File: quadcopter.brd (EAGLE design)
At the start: 140 x 140 mm, 65 parts, among them J1 AVR_SPI_PRG_6NS, Q1 N-CHANNEL_MOSFET, Q2 N-CHANNEL_MOSFET, Q3 N-CHANNEL_MOSFET, Q4 N-CHANNEL_MOSFET, U1 ATMEGA128RFA1

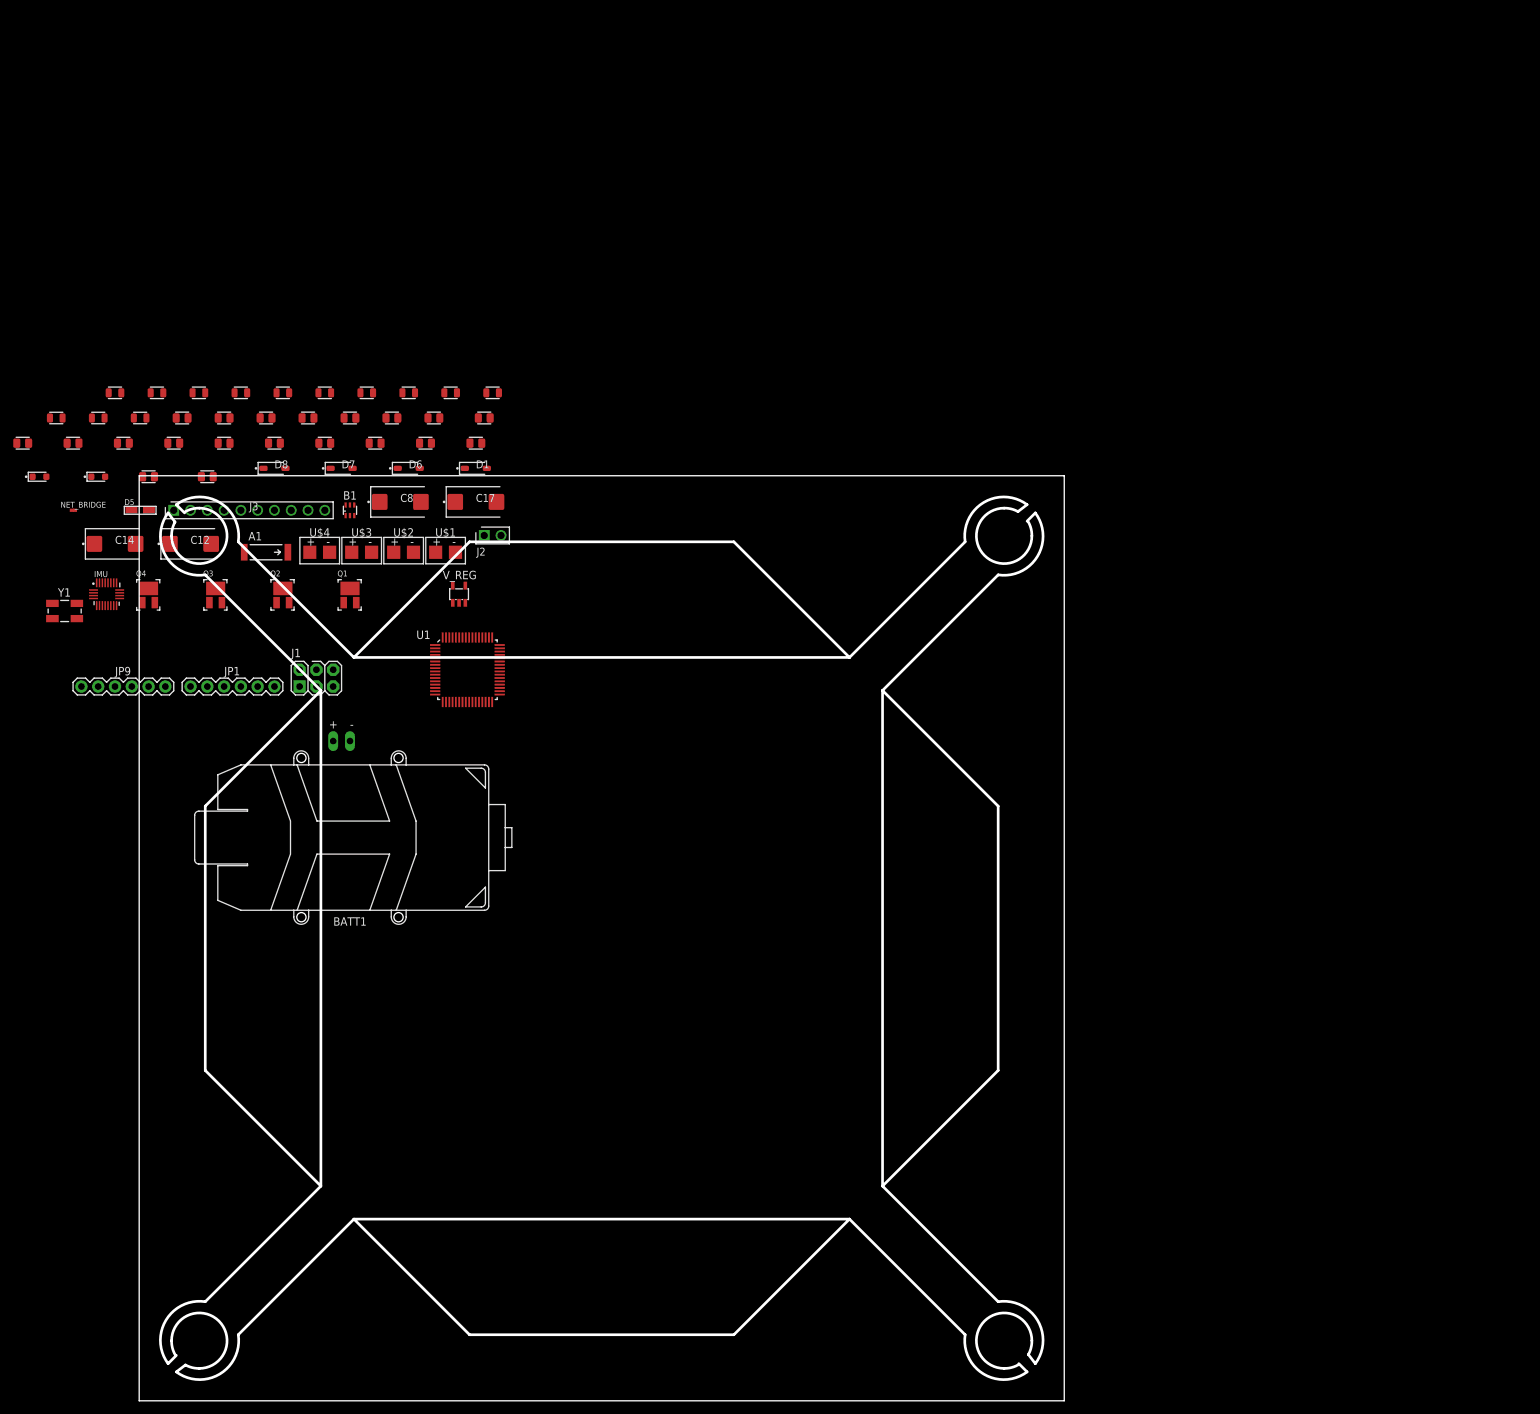
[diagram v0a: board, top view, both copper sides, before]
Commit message: Did board work, renamed flyback and filtered in schematic
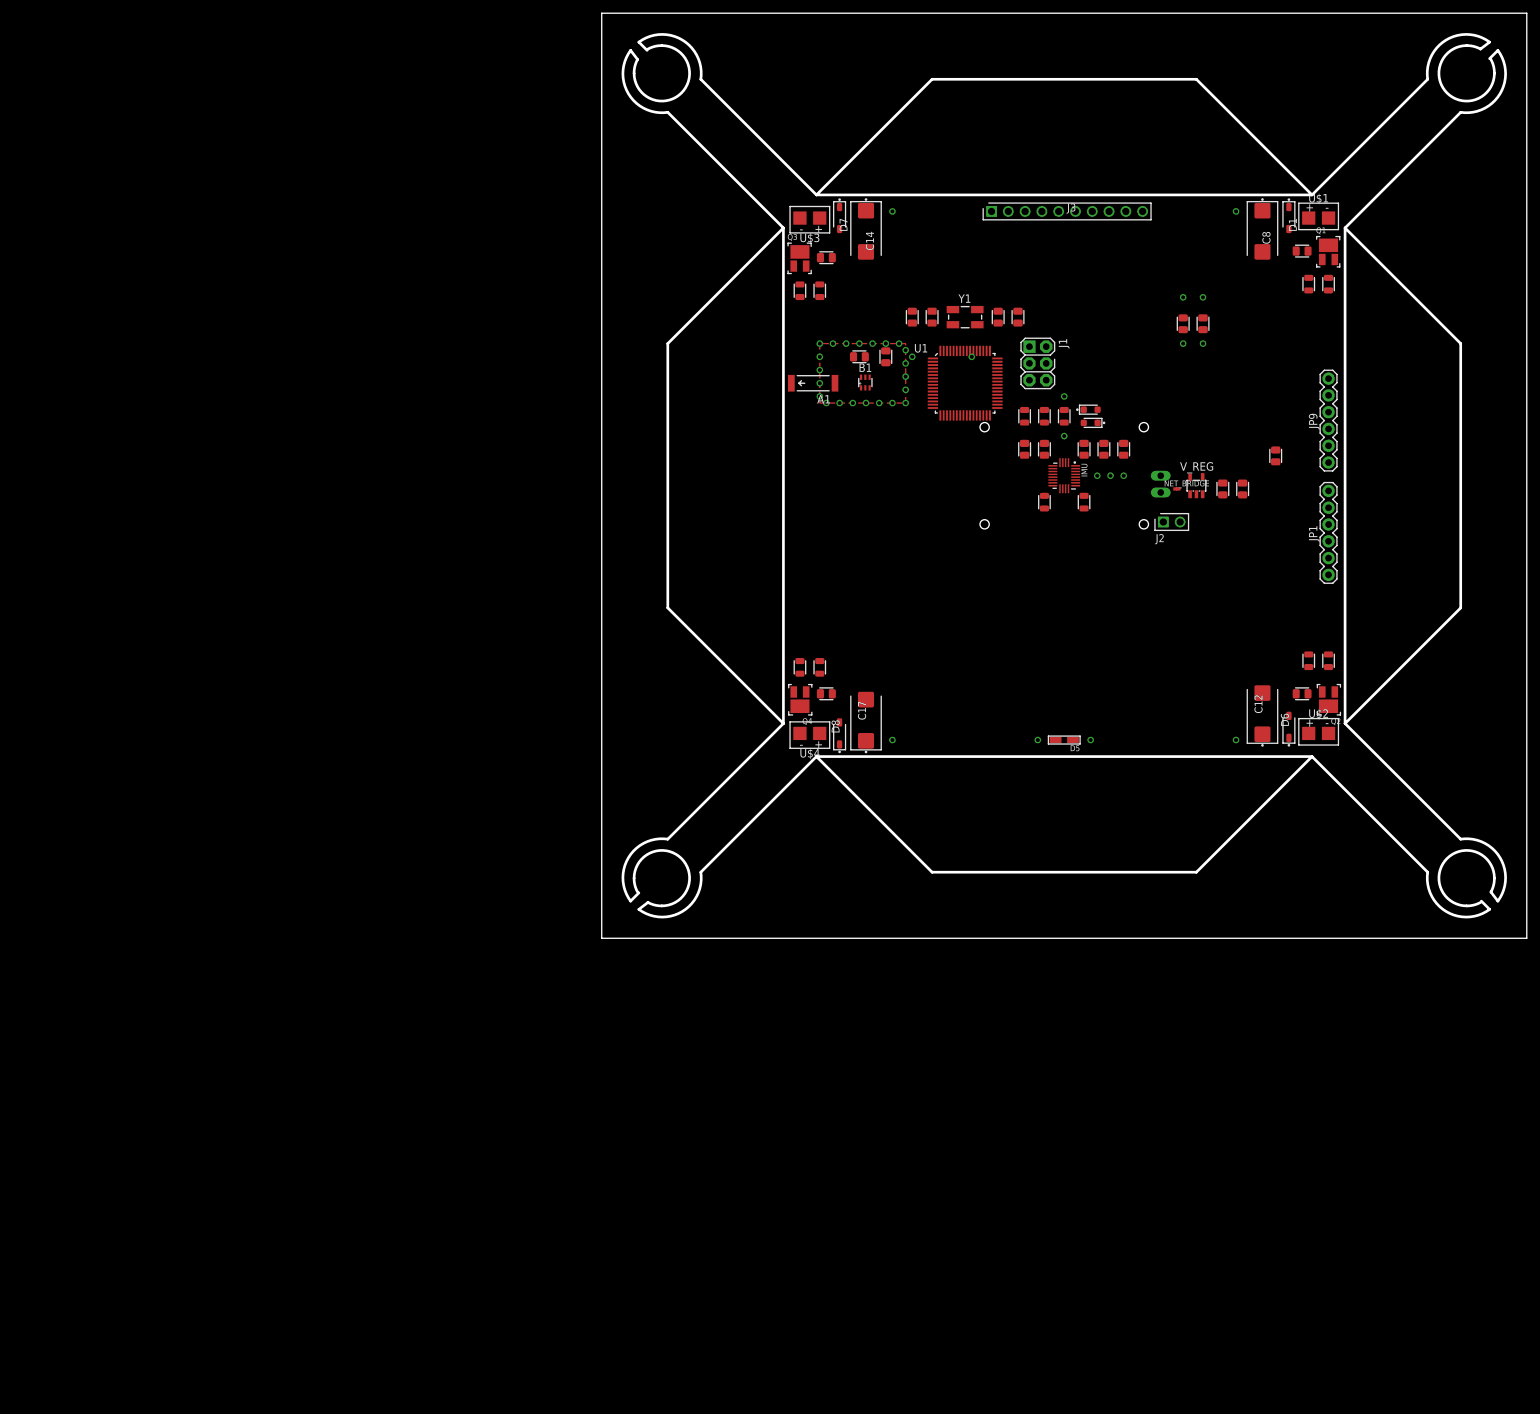
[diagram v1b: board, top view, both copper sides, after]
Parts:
- moved JP9 191.8 mm to (110.0, 72.0), turned to 90 degrees
- moved R3 190.6 mm to (107.0, 99.0), turned to 90 degrees
- moved R2 187.3 mm to (110.0, 99.0), turned to 90 degrees
- moved JP1 173.1 mm to (110.0, 55.0), turned to 90 degrees
- moved NET_BRIDGE 167.0 mm to (87.0, 68.0)
- moved C12 164.3 mm to (100.0, 34.0), turned to 90 degrees
- moved C24 160.9 mm to (97.0, 68.0), turned to 90 degrees
- moved LED3 159.4 mm to (74.0, 80.0)
- moved Q2 159.1 mm to (110.0, 36.0), turned to 180 degrees
- moved Q1 156.9 mm to (110.0, 104.0)
- moved C23 151.5 mm to (94.0, 68.0), turned to 90 degrees
- moved C22 151.4 mm to (79.0, 74.0), turned to 90 degrees
- moved LED2 150.4 mm to (74.0, 78.0), turned to 180 degrees
- moved C6 148.9 mm to (60.0, 94.0), turned to 90 degrees
- moved R7 148.2 mm to (107.0, 42.0), turned to 270 degrees
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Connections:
- removed net FILTERED: Q1.1, Q2.1, Q3.1, Q4.1, R10.2, R11.2, R2.2, R3.2, R4.2, R7.2, R8.2, R9.2
- removed net FLYBACK: D1.A, D6.A, D7.A, D8.A, Q1.3, Q2.3, Q3.3, Q4.3, U$1.V-, U$2.V-, U$3.V-, U$4.V-
- new net FILTERED1: Q1.1, R2.2, R3.2
- new net FILTERED2: Q2.1, R4.2, R7.2
- new net FILTERED3: Q3.1, R8.2, R9.2
- new net FILTERED4: Q4.1, R10.2, R11.2
- new net FLYBACK1: D1.A, Q1.3, U$1.V-
- new net FLYBACK2: D6.A, Q2.3, U$2.V-
- new net FLYBACK3: D7.A, Q3.3, U$3.V-
- new net FLYBACK4: D8.A, Q4.3, U$4.V-
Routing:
- added copper zone on layer 1, net GND
- added copper zone on layer 15, net GND
- added copper zone on layer 2, net GND
- added copper zone on layer 2, net VBAT
- added copper zone on layer 2, net VCC

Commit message: board before auto-routing
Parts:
- moved C24 6.37 mm to (92.8, 72.8), turned to 0 degrees
- moved C23 4.04 mm to (92.5, 64.2), turned to 0 degrees
- moved C21 3.82 mm to (76.8, 70.2)
- moved C18 3.51 mm to (63.8, 70.5)
- moved C20 2.85 mm to (75.8, 74.8)
- moved NET_BRIDGE 2.80 mm to (89.5, 69.2), turned to 270 degrees
- moved V_REG 2.75 mm to (92.8, 68.5)
- moved C19 2.61 mm to (64.5, 74.8)
- moved R13 2.57 mm to (75.2, 64.8)
- moved R12 2.36 mm to (65.0, 64.8)
- moved C9 1.82 mm to (37.2, 87.5), turned to 90 degrees
- moved Y1 1.25 mm to (55.0, 95.2)
- moved A1 0.75 mm to (32.0, 83.2)
- moved C11 0.71 mm to (42.5, 87.5)
- moved C22 0.25 mm to (79.0, 74.2)
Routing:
- added copper zone on layer 2, net N$20
- added copper zone on layer 15, net N$21
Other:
- board size 140 x 140 mm -> 133.6 x 133.6 mm
- board text added: "(res)"
- board text added: "BAT_GND"
- board text added: "DTR"
- board text added: "GND"
- board text added: "PWM1"
- board text added: "PWM2"
- board text added: "PWM3"
- board text added: "PWM4"
- board text added: "RXI"
- board text added: "SCL"
- board text added: "SDA"
- board text added: "TX0"
- board text added: "VBAT"
- board text added: "VCC"

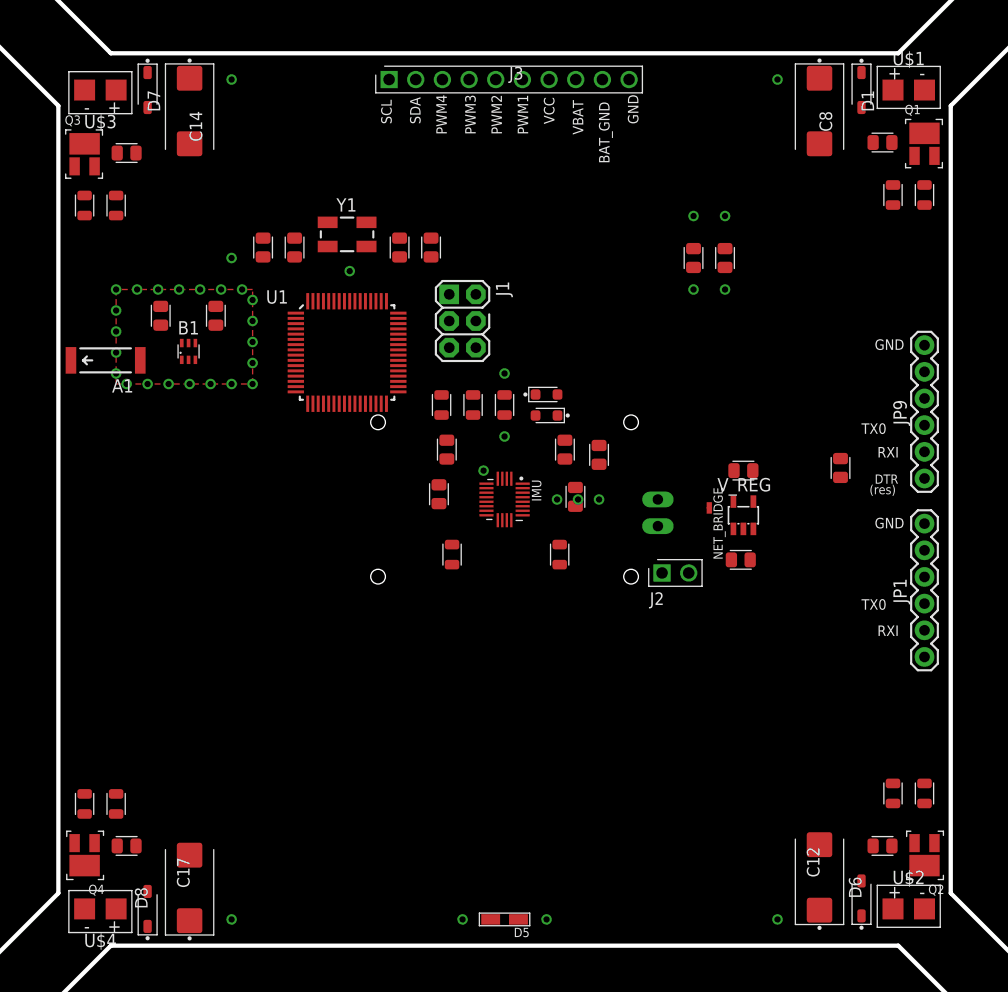
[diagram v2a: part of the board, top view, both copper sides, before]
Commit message: Routed and manually connected most wires. Waiting on piazza question before connecting the last few
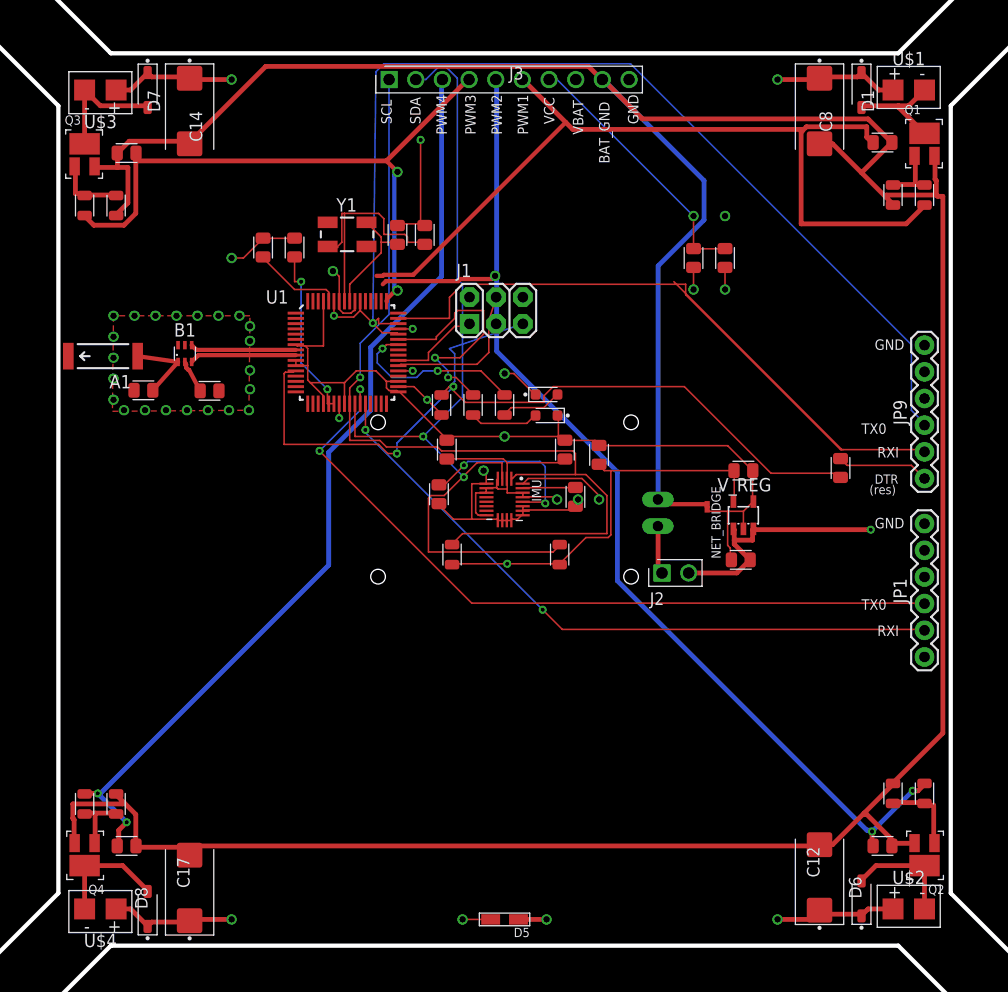
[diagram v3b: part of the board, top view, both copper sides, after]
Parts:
- moved C9 7.29 mm to (35.6, 80.4), turned to 180 degrees
- moved C11 7.18 mm to (41.9, 80.3), turned to 180 degrees
- moved J1 3.35 mm to (69.2, 88.0), turned to 0 degrees
- moved C5 1.34 mm to (62.4, 95.2)
- moved C6 1.22 mm to (59.8, 95.2)
- moved A1 0.47 mm to (31.8, 83.7)
- moved B1 0.40 mm to (39.5, 83.9)
- moved NET_BRIDGE 0.22 mm to (89.3, 69.3)
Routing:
- net BAT_GND: track 0.00 -> 318.6 mm
- net GND: track 0.00 -> 143.4 mm, vias 30 -> 32
- net VCC: track 0.00 -> 116.1 mm, vias 5 -> 9
- net PWM2: track 0.00 -> 106.3 mm, vias 0 -> 3
- net RX0: track 0.00 -> 97.6 mm, vias 0 -> 1
- net PWM4: track 0.00 -> 89.7 mm, vias 0 -> 2
- net SCL: track 0.00 -> 88.9 mm, vias 0 -> 1
- net SDA: track 0.00 -> 83.9 mm, vias 0 -> 2
- net RESET: track 0.00 -> 82.9 mm, vias 0 -> 2
- net TX0: track 0.00 -> 82.7 mm
- net PWM1: track 0.00 -> 82.3 mm
- net VBAT: track 0.00 -> 75.0 mm, vias 5 -> 6
- net N$9: track 0.00 -> 72.5 mm, vias 0 -> 2
- net N$12: track 0.00 -> 63.8 mm, vias 0 -> 2
- net PWM3: track 0.00 -> 61.1 mm, vias 0 -> 2
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
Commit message: finished routing
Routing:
- net PWM2: track 106.3 -> 154.7 mm, vias 3 -> 2
- net PWM4: track 89.7 -> 121.1 mm
- net TX0: track 82.7 -> 59.5 mm
- net PWM3: track 61.1 -> 76.3 mm, vias 2 -> 0
- net PWM1: track 82.3 -> 84.2 mm, vias 0 -> 2

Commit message: finished routing
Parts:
- moved R13 13.7 mm to (67.2, 75.8), turned to 0 degrees
- moved C19 6.65 mm to (71.0, 75.9), turned to 0 degrees
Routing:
- net VCC: track 116.1 -> 131.1 mm, vias 9 -> 13
- net SDA: track 83.9 -> 70.7 mm
- net GND: track 143.4 -> 152.5 mm, vias 32 -> 31
